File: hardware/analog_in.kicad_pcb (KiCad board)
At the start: 2 copper layers, 30 x 35 mm, 37 parts, among them P1 CON-SENSOR2, P2 CONN_5, P3 BOOT, P4 DEBUG, U1 XMC1XXX24, U2 TLV272IS, U3 DRILL, U4 DRILL, U5 DRILL, U6 DRILL

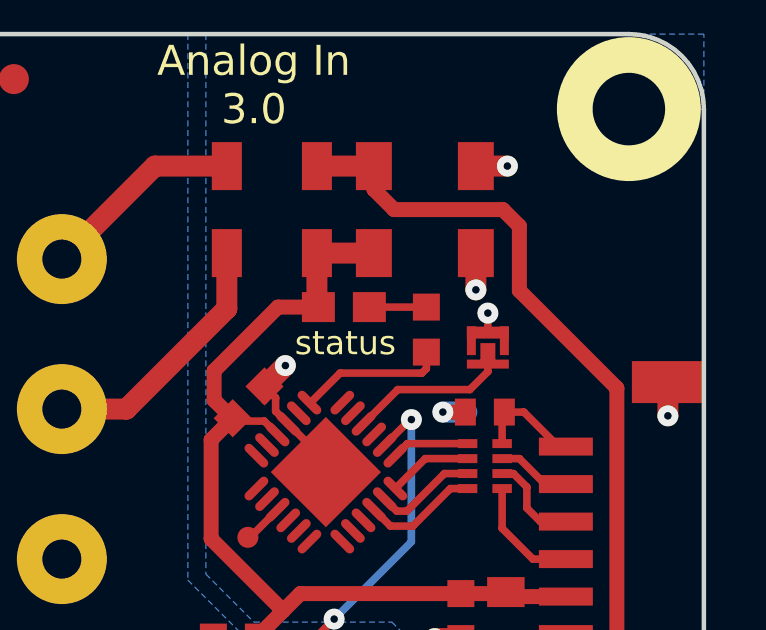
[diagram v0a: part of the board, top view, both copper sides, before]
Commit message: change led position
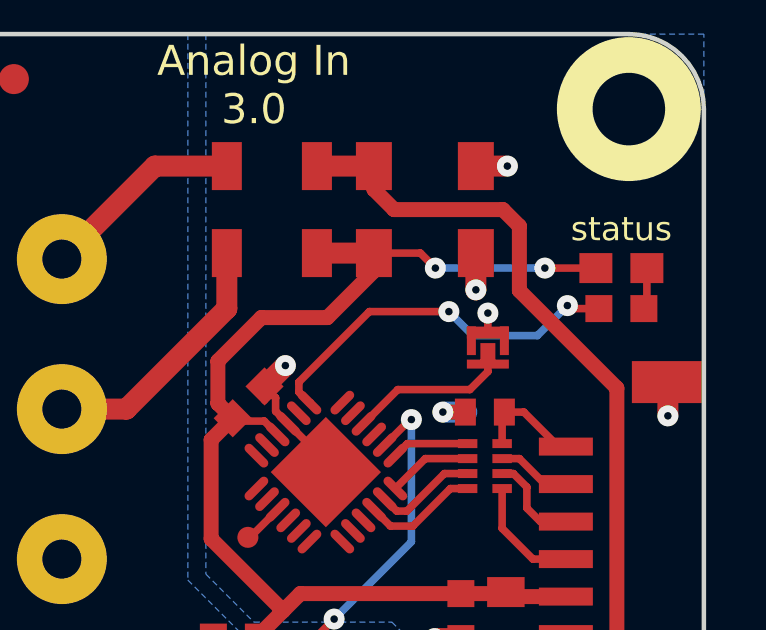
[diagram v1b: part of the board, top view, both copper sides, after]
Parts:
- moved D3 9.34 mm to (202.8, 102.4)
- moved R8 6.54 mm to (202.8, 103.8), turned to 0 degrees
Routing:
- net 3V3: track 31.6 -> 40.4 mm, vias 0 -> 2
- net Net-(R8-Pad1): track 4.92 -> 12.6 mm, vias 0 -> 2
- net Net-(D3-Pad2): track 1.90 -> 1.39 mm
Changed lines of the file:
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@@
-(kicad_pcb (version 4) (host pcbnew 4.0.2+dfsg1-stable)
+(kicad_pcb (version 4) (host pcbnew 4.0.7-e2-6376~58~ubuntu17.04.1)
   (general
     (links 65)
     (no_connects 0)
-    (area 174.644999 93.744999 282.49286 159.99)
+    (area 174.644999 93.744999 282.39286 160.39)
     (thickness 1.6)
     (drawings 21)
-    (tracks 195)
+    (tracks 209)
     (zones 0)
     (modules 37)
@@
   )
   (setup
-    (last_trace_width 0.7)
+    (last_trace_width 0.5)
     (user_trace_width 0.5)
     (user_trace_width 0.7)
@@
   )
   (module kicad-libraries:D0603E (layer F.Cu)
-    (at 193.5 103.7)
+    (at 202.75 102.4)
     (attr smd)
     (fp_text reference D3 (at 0.85 0.45) (layer F.Fab)
@@
   )
   (module kicad-libraries:C0603F (layer F.Cu)
-    (at 196.25 104.45 90)
+    (at 202.75 103.75)
     (attr smd)
-    (fp_text reference R8 (at 0.05 0.225 90) (layer F.Fab)
+    (fp_text reference R8 (at 0.05 0.225) (layer F.Fab)
       (effects (font (size 0.2 0.2) (thickness 0.05)))
     )
-    (fp_text value 1k (at 0.05 -0.375 90) (layer F.Fab)
+    (fp_text value 1k (at 0.05 -0.375) (layer F.Fab)
       (effects (font (size 0.2 0.2) (thickness 0.05)))
     )
@@
     (fp_line (start 1.45034 0.65024) (end -1.45034 0.65024) (layer F.Fab) (width 0.001))
     (fp_line (start -1.45034 0.65024) (end -1.45034 -0.65024) (layer F.Fab) (width 0.001))
-    (pad 1 smd rect (at -0.75 0 90) (size 0.9 0.9) (layers F.Cu F.Paste F.Mask)
+    (pad 1 smd rect (at -0.75 0) (size 0.9 0.9) (layers F.Cu F.Paste F.Mask)
       (net 20 "Net-(R8-Pad1)"))
-    (pad 2 smd rect (at 0.75 0 90) (size 0.9 0.9) (layers F.Cu F.Paste F.Mask)
+    (pad 2 smd rect (at 0.75 0) (size 0.9 0.9) (layers F.Cu F.Paste F.Mask)
       (net 17 "Net-(D3-Pad2)"))
     (model Capacitors_SMD/C_0603.wrl
@@
       (xy 1.301301 2.715081) (xy 1.302426 2.714986)) (layer B.SilkS) (width 0.01))
   )
-  (gr_text status (at 193.55 104.9) (layer F.SilkS)
+  (gr_text status (at 202.75 101.1) (layer F.SilkS)
     (effects (font (size 0.8 0.8) (thickness 0.15)))
   )
@@
   (gr_arc (start 178 127.1) (end 178 129.6) (angle 90) (layer Edge.Cuts) (width 0.15))
   (gr_arc (start 178 97.1) (end 175.5 97.1) (angle 90) (layer Edge.Cuts) (width 0.15))
+  (segment (start 194.50074 101.9) (end 194.50074 102.49926) (width 0.5) (layer F.Cu) (net 1))
+  (segment (start 194.50074 102.49926) (end 192.95 104.05) (width 0.5) (layer F.Cu) (net 1))
+  (segment (start 189.3 106.91066) (end 189.79467 107.40533) (width 0.5) (layer F.Cu) (net 1))
+  (segment (start 189.3 105.5) (end 189.3 106.91066) (width 0.5) (layer F.Cu) (net 1))
+  (segment (start 190.75 104.05) (end 189.3 105.5) (width 0.5) (layer F.Cu) (net 1))
+  (segment (start 192.95 104.05) (end 190.75 104.05) (width 0.5) (layer F.Cu) (net 1))
+  (segment (start 201.8999 102.4) (end 200.2 102.4) (width 0.254) (layer F.Cu) (net 1))
+  (segment (start 196.05 101.9) (end 194.50074 101.9) (width 0.254) (layer F.Cu) (net 1))
+  (segment (start 196.55 102.4) (end 196.05 101.9) (width 0.254) (layer F.Cu) (net 1))
+  (via (at 196.55 102.4) (size 0.7) (drill 0.25) (layers F.Cu B.Cu) (net 1))
+  (segment (start 200.2 102.4) (end 196.55 102.4) (width 0.254) (layer B.Cu) (net 1))
+  (via (at 200.2 102.4) (size 0.7) (drill 0.25) (layers F.Cu B.Cu) (net 1))
   (segment (start 189.79467 107.40533) (end 189.78033 107.40533) (width 0.7) (layer F.Cu) (net 1))
-  (segment (start 189.78033 107.40533) (end 189.175 106.8) (width 0.5) (layer F.Cu) (net 1))
-  (segment (start 189.175 106.8) (end 189.175 105.825) (width 0.5) (layer F.Cu) (net 1))
-  (segment (start 189.175 105.825) (end 191.3 103.7) (width 0.5) (layer F.Cu) (net 1))
-  (segment (start 191.3 103.7) (end 192.6499 103.7) (width 0.5) (layer F.Cu) (net 1))
-  (segment (start 192.60114 101.9) (end 192.60114 103.65124) (width 0.7) (layer F.Cu) (net 1))
-  (segment (start 192.60114 103.65124) (end 192.6499 103.7) (width 0.7) (layer F.Cu) (net 1))
   (segment (start 189.79467 107.5) (end 190.846447 107.5) (width 0.254) (layer F.Cu) (net 1))
   (segment (start 190.846447 107.5) (end 191.291332 107.944885) (width 0.254) (layer F.Cu) (net 1))
@@
   (segment (start 200.8007 108.2507) (end 200.9 108.35) (width 0.254) (layer F.Cu) (net 16))
   (segment (start 200.8007 108.2507) (end 200.9 108.35) (width 0.254) (layer F.Cu) (net 16))
-  (segment (start 196.25 103.7) (end 194.3501 103.7) (width 0.254) (layer F.Cu) (net 17))
+  (segment (start 203.6001 102.4) (end 203.6001 103.6499) (width 0.254) (layer F.Cu) (net 17))
+  (segment (start 203.6001 103.6499) (end 203.5 103.75) (width 0.254) (layer F.Cu) (net 17))
   (segment (start 198.3 105.6) (end 198.3 105.3) (width 0.254) (layer F.Cu) (net 18))
   (segment (start 198.3 105.3) (end 198.3 105.2) (width 0.254) (layer F.Cu) (net 18))
@@
   (segment (start 190.3 111.375) (end 190.371447 111.375) (width 0.254) (layer F.Cu) (net 19))
   (segment (start 190.371447 111.375) (end 191.291332 110.455115) (width 0.254) (layer F.Cu) (net 19))
+  (segment (start 192.351992 106.884225) (end 192 106.532233) (width 0.254) (layer F.Cu) (net 20))
+  (segment (start 192 106.532233) (end 192 106.2) (width 0.254) (layer F.Cu) (net 20))
+  (segment (start 201.05 103.75) (end 202 103.75) (width 0.254) (layer F.Cu) (net 20))
+  (segment (start 200.95 103.65) (end 201.05 103.75) (width 0.254) (layer F.Cu) (net 20))
+  (via (at 200.95 103.65) (size 0.7) (drill 0.25) (layers F.Cu B.Cu) (net 20))
+  (segment (start 199.95 104.65) (end 200.95 103.65) (width 0.254) (layer B.Cu) (net 20))
+  (segment (start 197.8 104.65) (end 199.95 104.65) (width 0.254) (layer B.Cu) (net 20))
+  (segment (start 197 103.85) (end 197.8 104.65) (width 0.254) (layer B.Cu) (net 20))
+  (via (at 197 103.85) (size 0.7) (drill 0.25) (layers F.Cu B.Cu) (net 20))
+  (segment (start 194.35 103.85) (end 197 103.85) (width 0.254) (layer F.Cu) (net 20))
+  (segment (start 192 106.2) (end 194.35 103.85) (width 0.254) (layer F.Cu) (net 20))
   (segment (start 192.351992 106.884225) (end 192.390775 106.884225) (width 0.254) (layer F.Cu) (net 20))
-  (segment (start 192.390775 106.884225) (end 193.375 105.9) (width 0.254) (layer F.Cu) (net 20))
-  (segment (start 193.375 105.9) (end 196.1 105.9) (width 0.254) (layer F.Cu) (net 20))
-  (segment (start 196.1 105.9) (end 196.25 105.75) (width 0.254) (layer F.Cu) (net 20))
-  (segment (start 196.25 105.75) (end 196.25 105.2) (width 0.254) (layer F.Cu) (net 20))
   (segment (start 197.625 108.2507) (end 195.617067 108.2507) (width 0.254) (layer F.Cu) (net 21))
   (segment (start 195.617067 108.2507) (end 195.215775 108.651992) (width 0.254) (layer F.Cu) (net 21))

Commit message: Fix 3d model (R0603F instead of C0603F)
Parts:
- R8: footprint kicad-libraries:C0603F -> kicad-libraries:R0603F
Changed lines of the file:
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@@
-(kicad_pcb (version 4) (host pcbnew 4.0.7-e2-6376~58~ubuntu17.04.1)
+(kicad_pcb (version 4) (host pcbnew 4.0.2+dfsg1-stable)
   (general
     (links 65)
     (no_connects 0)
-    (area 174.644999 93.744999 282.39286 160.39)
+    (area 175.424999 94.524999 205.575001 129.675001)
     (thickness 1.6)
     (drawings 21)
@@
   )
   (setup
-    (last_trace_width 0.5)
+    (last_trace_width 0.254)
     (user_trace_width 0.5)
     (user_trace_width 0.7)
@@
       (net 19 "Net-(P4-Pad1)"))
   )
-  (module kicad-libraries:C0603F (layer F.Cu)
-    (at 202.75 103.75)
-    (attr smd)
-    (fp_text reference R8 (at 0.05 0.225) (layer F.Fab)
-      (effects (font (size 0.2 0.2) (thickness 0.05)))
-    )
-    (fp_text value 1k (at 0.05 -0.375) (layer F.Fab)
-      (effects (font (size 0.2 0.2) (thickness 0.05)))
-    )
-    (fp_line (start -1.45034 -0.65024) (end 1.45034 -0.65024) (layer F.Fab) (width 0.001))
-    (fp_line (start 1.45034 -0.65024) (end 1.45034 0.65024) (layer F.Fab) (width 0.001))
-    (fp_line (start 1.45034 0.65024) (end -1.45034 0.65024) (layer F.Fab) (width 0.001))
-    (fp_line (start -1.45034 0.65024) (end -1.45034 -0.65024) (layer F.Fab) (width 0.001))
-    (pad 1 smd rect (at -0.75 0) (size 0.9 0.9) (layers F.Cu F.Paste F.Mask)
-      (net 20 "Net-(R8-Pad1)"))
-    (pad 2 smd rect (at 0.75 0) (size 0.9 0.9) (layers F.Cu F.Paste F.Mask)
-      (net 17 "Net-(D3-Pad2)"))
-    (model Capacitors_SMD/C_0603.wrl
-      (at (xyz 0 0 0))
-      (scale (xyz 1 1 1))
-      (rotate (xyz 0 0 0))
-    )
-  )
   (module kicad-libraries:4X0402 (layer F.Cu)
     (at 198.2 109 90)
@@
       (xy 1.301301 2.715081) (xy 1.302426 2.714986)) (layer B.SilkS) (width 0.01))
   )
+  (module kicad-libraries:R0603F (layer F.Cu)
+    (at 202.75 103.75)
+    (attr smd)
+    (fp_text reference R8 (at 0.05 0.225) (layer F.Fab)
+      (effects (font (size 0.2 0.2) (thickness 0.05)))
+    )
+    (fp_text value 1k (at 0.05 -0.375) (layer F.Fab)
+      (effects (font (size 0.2 0.2) (thickness 0.05)))
+    )
+    (fp_line (start -1.45034 -0.65024) (end 1.45034 -0.65024) (layer F.Fab) (width 0.001))
+    (fp_line (start 1.45034 -0.65024) (end 1.45034 0.65024) (layer F.Fab) (width 0.001))
+    (fp_line (start 1.45034 0.65024) (end -1.45034 0.65024) (layer F.Fab) (width 0.001))
+    (fp_line (start -1.45034 0.65024) (end -1.45034 -0.65024) (layer F.Fab) (width 0.001))
+    (pad 1 smd rect (at -0.75 0) (size 0.9 0.9) (layers F.Cu F.Paste F.Mask)
+      (net 20 "Net-(R8-Pad1)"))
+    (pad 2 smd rect (at 0.75 0) (size 0.9 0.9) (layers F.Cu F.Paste F.Mask)
+      (net 17 "Net-(D3-Pad2)"))
+    (model Resistors_SMD/R_0603.wrl
+      (at (xyz 0 0 0))
+      (scale (xyz 1 1 1))
+      (rotate (xyz 0 0 0))
+    )
+  )
   (gr_text status (at 202.75 101.1) (layer F.SilkS)

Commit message: specify processor type
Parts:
- U1: value XMC1XXX24 -> XMC110024
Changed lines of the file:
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@@
-(kicad_pcb (version 4) (host pcbnew 4.0.2+dfsg1-stable)
+(kicad_pcb (version 4) (host pcbnew 4.0.7-e2-6376~58~ubuntu17.04.1)
   (general
     (links 65)
     (no_connects 0)
-    (area 175.424999 94.524999 205.575001 129.675001)
+    (area 174.644999 93.744999 282.39286 160.39)
     (thickness 1.6)
     (drawings 21)
@@
       (effects (font (size 0.3 0.3) (thickness 0.075)))
     )
-    (fp_text value XMC1XXX24 (at 0 0.8 225) (layer F.Fab)
+    (fp_text value XMC110024 (at 0 0.8 225) (layer F.Fab)
       (effects (font (size 0.3 0.3) (thickness 0.075)))
     )
